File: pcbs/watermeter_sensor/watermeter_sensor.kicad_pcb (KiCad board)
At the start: 2 copper layers, 32.5 x 18 mm, 15 parts, among them J1 Conn_01x06, U1 LDC2112, U2 MCP1811A

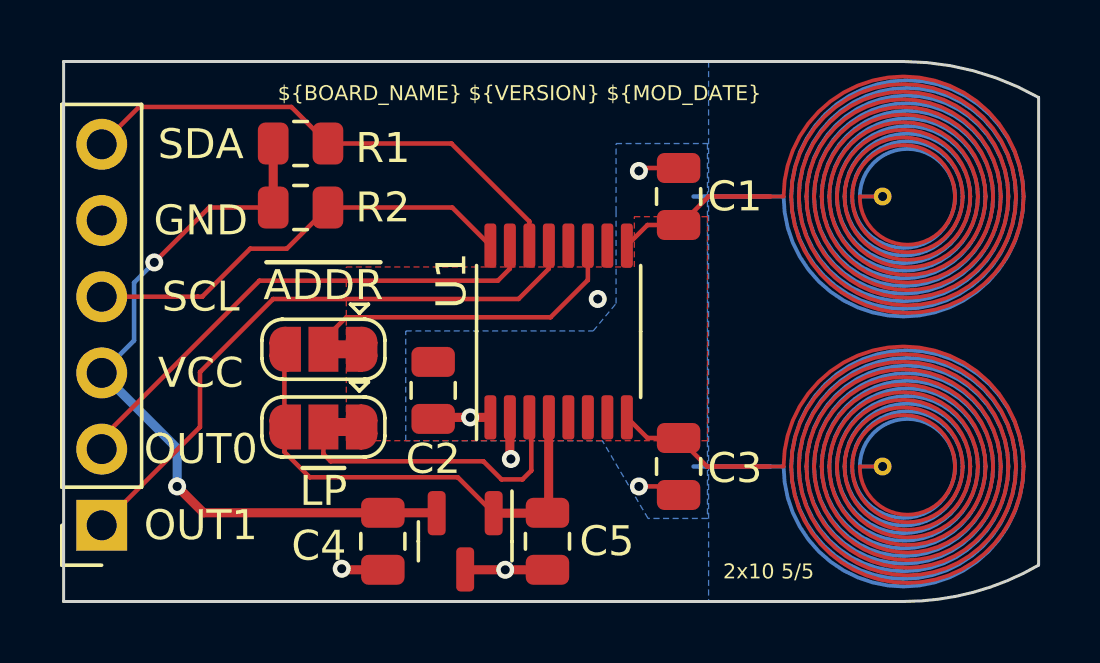
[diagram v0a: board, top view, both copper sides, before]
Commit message: chore: Update .gitignore, upgrade to KiCAD 8
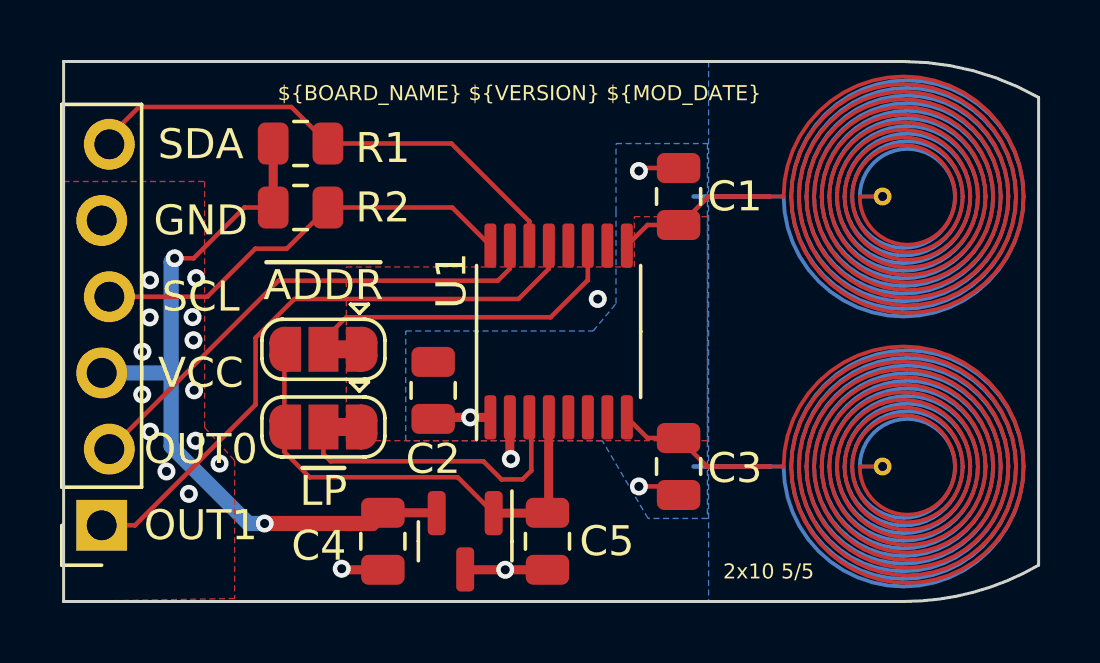
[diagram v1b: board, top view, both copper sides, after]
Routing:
- net GND: vias 4 -> 17

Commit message: PCB Changes v1.1: - changed LDO - some footprints changed to 0603
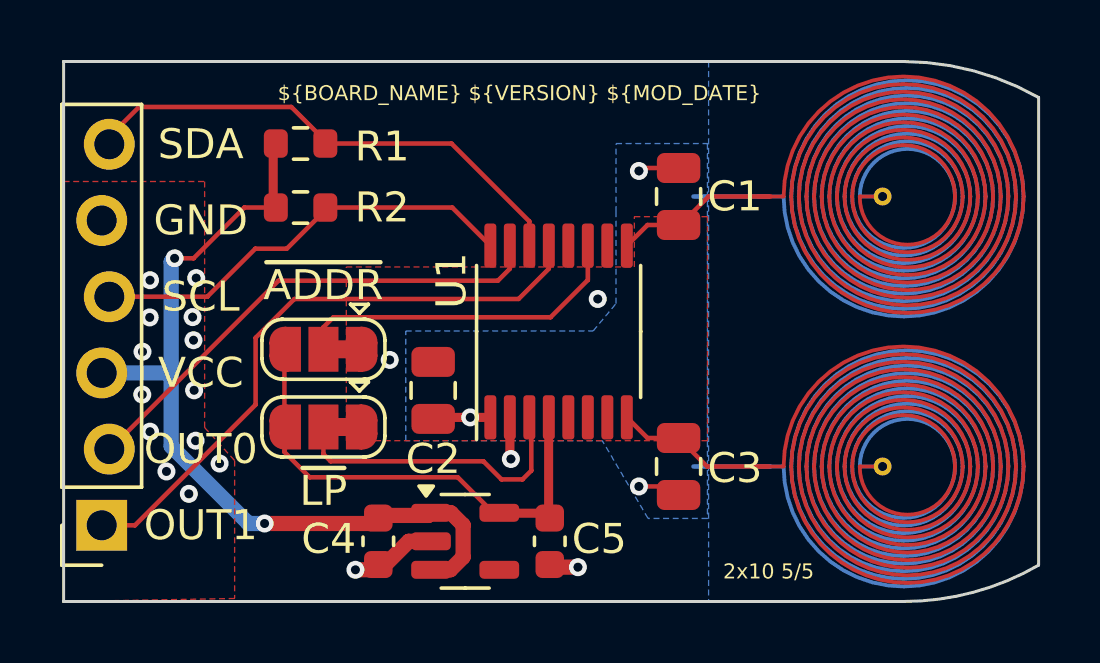
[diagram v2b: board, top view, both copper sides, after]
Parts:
- C4, C5: footprint Capacitor_SMD:C_0805_2012Metric -> Capacitor_SMD:C_0603_1608Metric
- R1, R2: footprint Resistor_SMD:R_0805_2012Metric -> Resistor_SMD:R_0603_1608Metric
- U2: value MCP1811A -> AP7354-18W5; footprint Package_TO_SOT_SMD:SOT-23 -> Package_TO_SOT_SMD:TSOT-23-5
- moved C4 0.15 mm to (110.5, 98.0)
- moved C5 0.08 mm to (116.2, 98.0)
- turned U2 to 0 degrees
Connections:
- U2 pad 1: +1V8 -> VCC
- U2 pad 2: VCC -> GND
- U2 pad 3: GND -> VCC
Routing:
- net VCC: track 24.9 -> 27.8 mm
- net GND: track 5.54 -> 5.33 mm, vias 17 -> 18
